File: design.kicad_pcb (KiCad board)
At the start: 2 copper layers, 38 x 11 mm, 1 part, among them U1 TPS61099YFFT

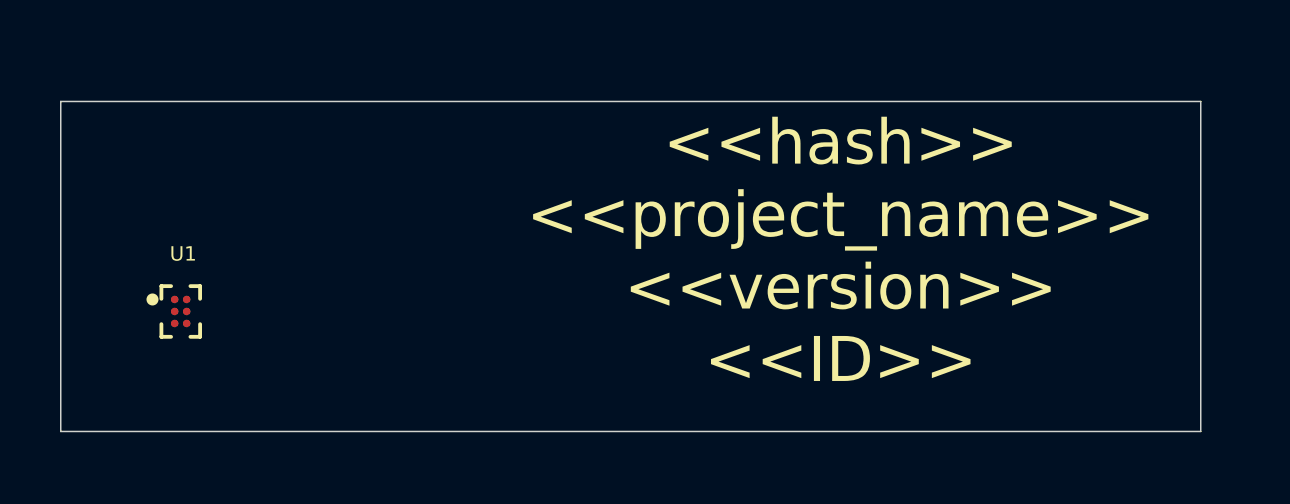
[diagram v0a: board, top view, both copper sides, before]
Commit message: PCB Add Date SilkScreen
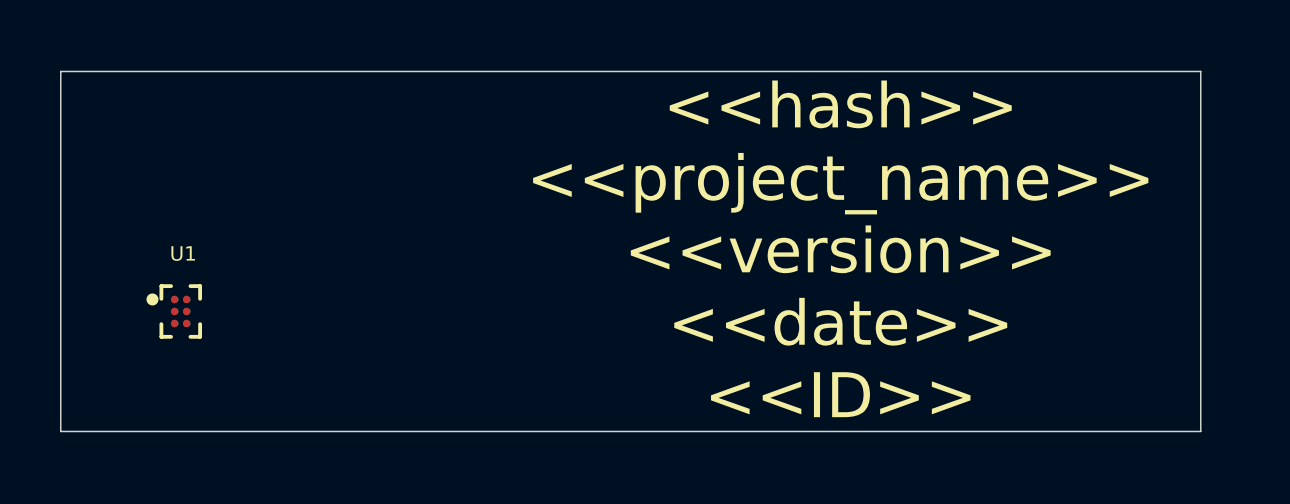
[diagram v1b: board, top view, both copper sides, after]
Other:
- board size 38 x 11 mm -> 38 x 12 mm
- board text added: "<<hash>> <<project_name>> <<version>> <<date>> <<ID>>"
- board text removed: "<<hash>> <<project_name>> <<version>> <<ID>>"
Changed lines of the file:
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@@
     )
   )
-  (gr_rect (start 143 89) (end 181 100) (layer "Edge.Cuts") (width 0.05) (fill none))
-  (gr_text "<<hash>>\n<<project_name>>\n<<version>>\n<<ID>>" (at 169 94) (layer "F.SilkS")
+  (gr_rect (start 143 88) (end 181 100) (layer "Edge.Cuts") (width 0.05) (fill none))
+  (gr_text "<<hash>>\n<<project_name>>\n<<version>>\n<<date>>\n<<ID>>" (at 169 94) (layer "F.SilkS")
     (effects (font (size 1.5 1.5) (thickness 0.3)))
   )
